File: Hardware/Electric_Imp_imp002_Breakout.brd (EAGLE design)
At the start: 43.2 x 45.7 mm, 42 parts, among them Q1 DMG2307L-7, Q2 PHOTOTRANSISTORPT17-21C-L41-T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, U1 imp002, U2 TPS62172, X1 USBSMD

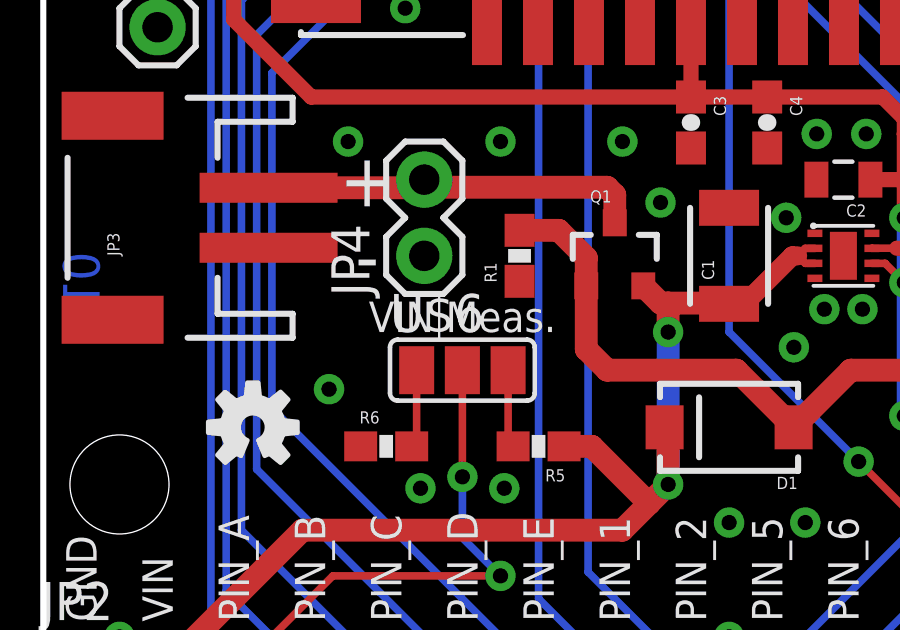
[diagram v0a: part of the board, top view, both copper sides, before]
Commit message: Fixed 3-way jumper name. Added PROD_ID to components lacking it. Added device name to phototransistor in schematic.
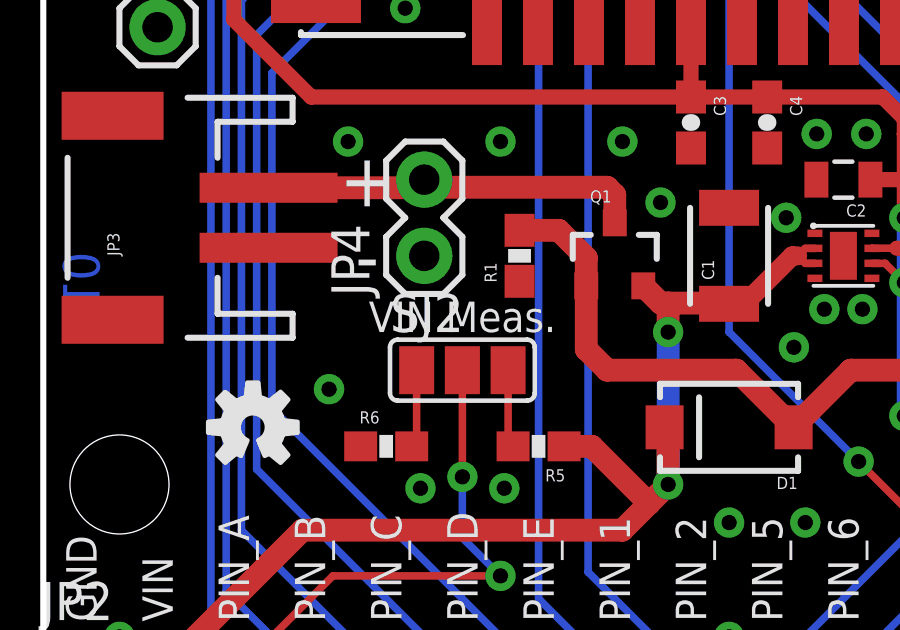
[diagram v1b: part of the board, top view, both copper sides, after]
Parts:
- Q1: value DMG2307L-7 -> DMG2307L
- renumbered U$6 to SJ2
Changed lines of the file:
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@@
 <setting verticaltext="up"/>
 </settings>
-<grid distance="0.05" unitdist="inch" unit="inch" style="dots" multiple="1" display="yes" altdistance="0.025" altunitdist="inch" altunit="inch"/>
+<grid distance="0.05" unitdist="inch" unit="inch" style="dots" multiple="1" display="yes" altdistance="0.005" altunitdist="inch" altunit="inch"/>
 <layers>
 <layer number="1" name="Top" color="4" fill="1" visible="yes" active="yes"/>
@@
 <text x="10.795" y="14.351" size="1.778" layer="21" font="vector" ratio="15" align="bottom-center">-</text>
 <text x="13.97" y="12.7" size="1.016" layer="21" font="vector" ratio="15" align="bottom-center">VIN Meas.</text>
+<rectangle x1="33.528" y1="23.0505" x2="34.544" y2="38.7985" layer="41"/>
 </plain>
 <attributes>
@@
 <attribute name="PROD_ID" value="IC-12130" x="49.53" y="20.32" size="1.778" layer="27" display="off"/>
 </element>
-<element name="C2" library="SparkFun-Passives" package="0805" value="22uF" x="26.67" y="17.78" rot="R180"/>
+<element name="C2" library="SparkFun-Passives" package="0805" value="22uF" x="26.67" y="17.78" rot="R180">
+<attribute name="PROD_ID" value="CAP-08402" x="26.67" y="17.78" size="1.778" layer="27" rot="R180" display="off"/>
+</element>
 <element name="L1" library="SparkFun-Passives" package="VLF4012A" value="2.2uH" x="30.48" y="17.399" rot="R90"/>
-<element name="U2" library="SparkFun-PowerIC" package="WSON-8-PAD" value="TPS62172" x="26.67" y="15.24" rot="R270"/>
+<element name="U2" library="SparkFun-PowerIC" package="WSON-8-PAD" value="TPS62172" x="26.67" y="15.24" rot="R270">
+<attribute name="PROD_ID" value="IC-11307" x="26.67" y="15.24" size="1.778" layer="27" rot="R270" display="off"/>
+</element>
 <element name="C1" library="SparkFun-Passives" package="1210" value="10uF" x="22.86" y="15.24" rot="R90"/>
 <element name="JP2" library="SparkFun-Connectors" package="1X02" value="M02PTH" x="1.27" y="1.27"/>
@@
 </element>
 <element name="JP4" library="SparkFun-Connectors" package="1X02" value="M02PTH" x="12.7" y="15.24" rot="R90"/>
-<element name="Q1" library="SparkFun-DiscreteSemi" package="SOT23-3" value="DMG2307L-7" x="19.05" y="15.24"/>
+<element name="Q1" library="SparkFun-DiscreteSemi" package="SOT23-3" value="DMG2307L" x="19.05" y="15.24">
+<attribute name="PROD_ID" value="TRANS-11308" x="19.05" y="15.24" size="1.778" layer="27" display="off"/>
+<attribute name="VALUE" value="2.5A/30V" x="19.05" y="15.24" size="1.778" layer="27" display="off"/>
+</element>
 <element name="JP3" library="SparkFun-Connectors" package="JST-2-SMD" value="M02-JST-2MM-SMT" x="3.81" y="16.51" rot="R90">
 <attribute name="PROD_ID" value="CONN-08352" x="3.81" y="16.51" size="1.778" layer="27" rot="R90" display="off"/>
 </element>
-<element name="C3" library="SparkFun-Capacitors" package="0603-CAP" value="100pF" x="21.59" y="19.685" rot="R270"/>
+<element name="C3" library="SparkFun-Capacitors" package="0603-CAP" value="100pF" x="21.59" y="19.685" rot="R270">
+<attribute name="PROD_ID" value="CAP-07883" x="21.59" y="19.685" size="1.778" layer="27" rot="R270" display="off"/>
+</element>
 <element name="C4" library="SparkFun-Capacitors" package="0603-CAP" value="1.0uF" x="24.13" y="19.685" rot="R270">
 <attribute name="PROD_ID" value="CAP-00868" x="24.13" y="19.685" size="1.778" layer="27" font="vector" ratio="15" rot="R270" display="off"/>
 </element>
-<element name="C5" library="SparkFun-Capacitors" package="0603-CAP" value="100pF" x="39.37" y="35.56"/>
+<element name="C5" library="SparkFun-Capacitors" package="0603-CAP" value="100pF" x="39.37" y="35.56">
+<attribute name="PROD_ID" value="CAP-07883" x="39.37" y="35.56" size="1.778" layer="27" display="off"/>
+</element>
 <element name="C6" library="SparkFun-Capacitors" package="0603-CAP" value="1.0uF" x="39.37" y="27.94">
 <attribute name="PROD_ID" value="CAP-00868" x="39.37" y="27.94" size="1.778" layer="27" font="vector" ratio="15" display="off"/>
@@
 <element name="Q2" library="SparkFun-DiscreteSemi" package="PT17-21C-L41-TR8" value="PHOTOTRANSISTORPT17-21C-L41-TR8" x="3.81" y="38.1" rot="R270">
 <attribute name="PROD_ID" value="TRANS-12141" x="3.81" y="38.1" size="1.778" layer="27" font="vector" ratio="15" rot="R270" display="off"/>
+<attribute name="DEVICE" value="PT17-21C-L41-TR8" x="3.81" y="38.1" size="1.778" layer="27" rot="R270" display="off"/>
 </element>
 <element name="D2" library="SparkFun-LED" package="LTST-C195KGJRKT" value="LED-RGLTST-C195KGJRKT" x="3.81" y="27.94" rot="R270">
@@
 <attribute name="PROD_ID" value="RES-00818" x="3.81" y="33.655" size="1.778" layer="27" font="vector" ratio="15" rot="R180" display="off"/>
 </element>
-<element name="R4" library="SparkFun-Resistors" package="0603-RES" value="33k" x="3.81" y="35.56" rot="R180"/>
+<element name="R4" library="SparkFun-Resistors" package="0603-RES" value="33k" x="3.81" y="35.56" rot="R180">
+<attribute name="PROD_ID" value="RES-08416" x="3.81" y="35.56" size="1.778" layer="27" rot="R180" display="off"/>
+</element>
 <element name="JP1" library="SparkFun-Connectors" package="1X15" value="M15" x="41.91" y="1.27" rot="R180"/>
 <element name="JP5" library="SparkFun-Connectors" package="1X01" value="M01PTH" x="3.81" y="22.86"/>
@@
 <attribute name="PROD_ID" value="DIO-08053" x="22.86" y="9.525" size="1.778" layer="27" font="vector" ratio="15" rot="R180" display="off"/>
 </element>
-<element name="U$6" library="SparkFun-Passives" package="PAD-JUMPER-3-NO_YES_SILK_FULL_BOX" value="JUMPER-PAD-3-NOFULL_BOX_SILK" x="13.97" y="11.43"/>
-<element name="R5" library="SparkFun-Resistors" package="0603-RES" value="33k" x="16.51" y="8.89" rot="R180"/>
-<element name="R6" library="SparkFun-Resistors" package="0603-RES" value="62k" x="11.43" y="8.89"/>
-<element name="C7" library="SparkFun-Capacitors" package="0603-CAP" value="100pF" x="39.37" y="38.1" rot="R180"/>
+<element name="SJ2" library="SparkFun-Passives" package="PAD-JUMPER-3-NO_YES_SILK_FULL_BOX" value="JUMPER-PAD-3-NOFULL_BOX_SILK" x="13.97" y="11.43"/>
+<element name="R5" library="SparkFun-Resistors" package="0603-RES" value="33k" x="16.51" y="8.89" rot="R180">
+<attribute name="PROD_ID" value="RES-08416" x="16.51" y="8.89" size="1.778" layer="27" rot="R180" display="off"/>
+</element>
+<element name="R6" library="SparkFun-Resistors" package="0603-RES" value="62k" x="11.43" y="8.89">
+<attribute name="PROD_ID" value="RES-09993" x="11.43" y="8.89" size="1.778" layer="27" display="off"/>
+</element>
+<element name="C7" library="SparkFun-Capacitors" package="0603-CAP" value="100pF" x="39.37" y="38.1" rot="R180">
+<attribute name="PROD_ID" value="CAP-07883" x="39.37" y="38.1" size="1.778" layer="27" rot="R180" display="off"/>
+</element>
 <element name="TP1" library="SparkFun-Passives" package="PAD.03X.05" value="TEST-POINT3X5" x="3.81" y="38.1" rot="MR0"/>
 <element name="TP2" library="SparkFun-Passives" package="PAD.03X.05" value="TEST-POINT3X5" x="3.81" y="35.56" rot="MR0"/>
@@
 <signal name="PIN_A">
 <contactref element="U1" pad="8"/>
-<contactref element="U$6" pad="2"/>
+<contactref element="SJ2" pad="2"/>
 <contactref element="JP1" pad="15"/>
 <via x="11.43" y="32.004" extent="1-16" drill="0.508"/>
@@
 <signal name="N$6">
 <contactref element="R5" pad="2"/>
-<contactref element="U$6" pad="3"/>
+<contactref element="SJ2" pad="3"/>
 <wire x1="15.494" y1="11.43" x2="15.494" y2="9.056" width="0.254" layer="1"/>
 <wire x1="15.494" y1="9.056" x2="15.66" y2="8.89" width="0.254" layer="1"/>
 </signal>
 <signal name="N$7">
-<contactref element="U$6" pad="1"/>
+<contactref element="SJ2" pad="1"/>
 <contactref element="R6" pad="2"/>
 <wire x1="12.446" y1="11.43" x2="12.446" y2="9.056" width="0.254" layer="1"/>

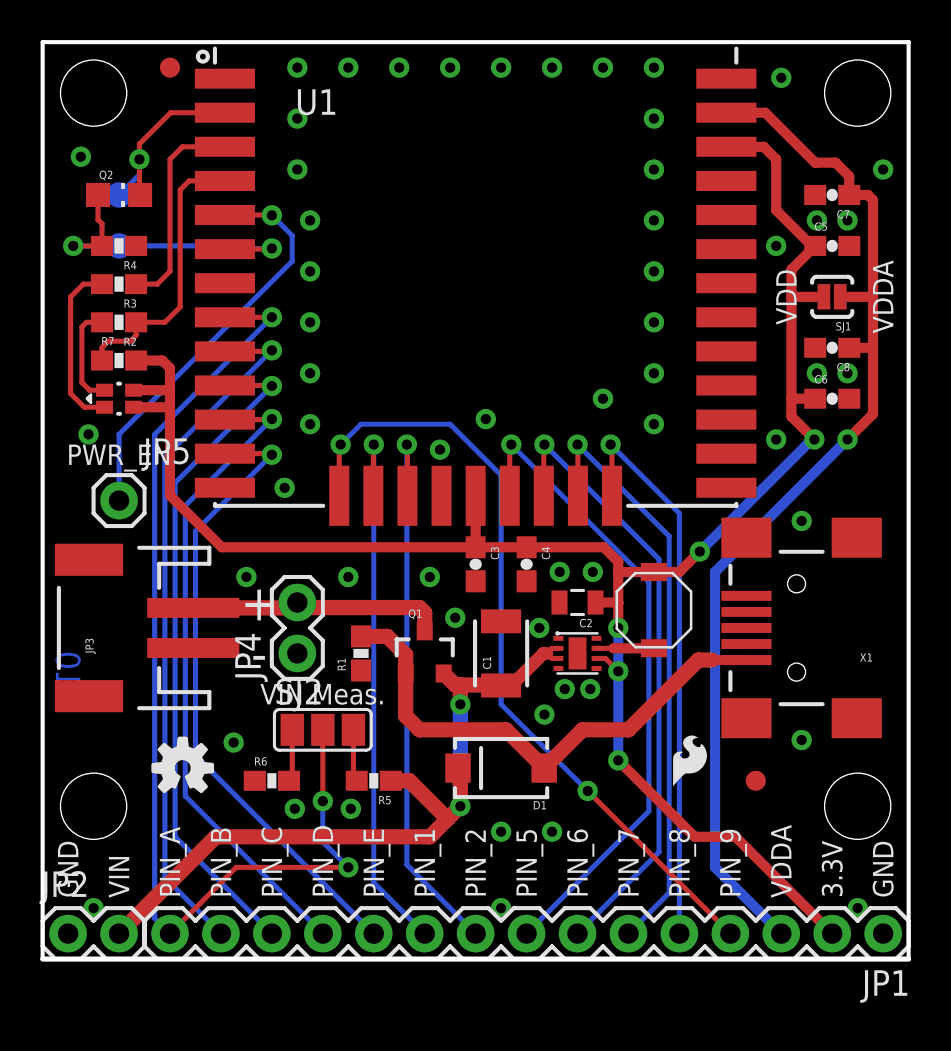
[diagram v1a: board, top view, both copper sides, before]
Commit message: Fixed issues from GitHub for reds.
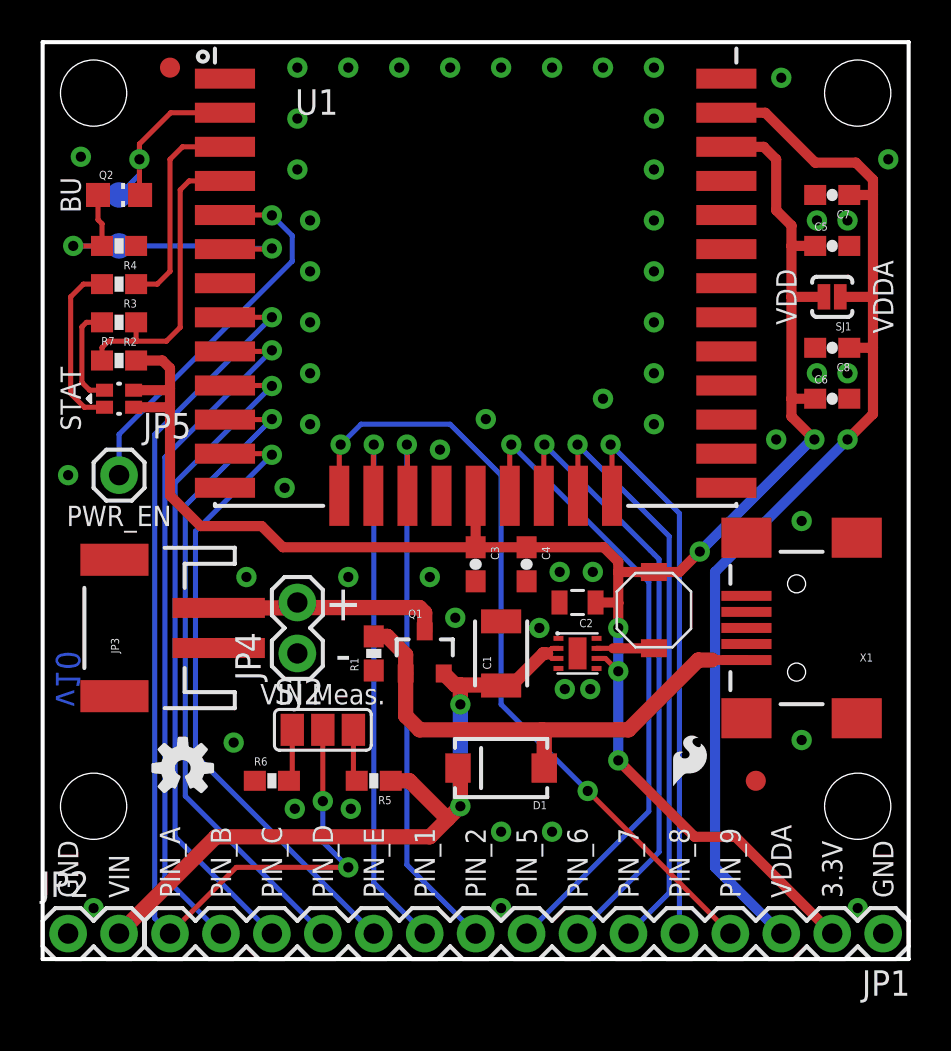
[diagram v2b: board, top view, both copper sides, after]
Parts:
- Q2: value PHOTOTRANSISTORPT17-21C-L41-TR8 -> PT17-21C-L41-TR8
- moved JP3 1.27 mm to (5.08, 16.5)
- moved JP5 1.27 mm to (3.81, 24.1)
- moved R1 0.64 mm to (16.5, 15.2)
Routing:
- net VBAT: track 12.8 -> 11.5 mm
- net POWER_EN: track 20.6 -> 19.3 mm
- net LED_R: track 14.0 -> 15.2 mm
- net VDDA: track 53.8 -> 54.9 mm
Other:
- board text added: "BU"
- board text added: "STAT"
